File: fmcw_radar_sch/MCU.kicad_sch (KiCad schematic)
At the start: 0 parts

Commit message: minor changes
minorchanges
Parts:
- added U1: STM32F100CBTx, Package_QFP:LQFP-48_7x7mm_P0.5mm, symbol MCU_ST_STM32F1:STM32F100CBTx
- added U2: ADF4372BCCZ, CC-48-4_ADI, symbol Analog Devices:ADF4372BCCZ
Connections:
- new net: U1.23 (VSS), U1.35 (VSS), U1.47 (VSS)

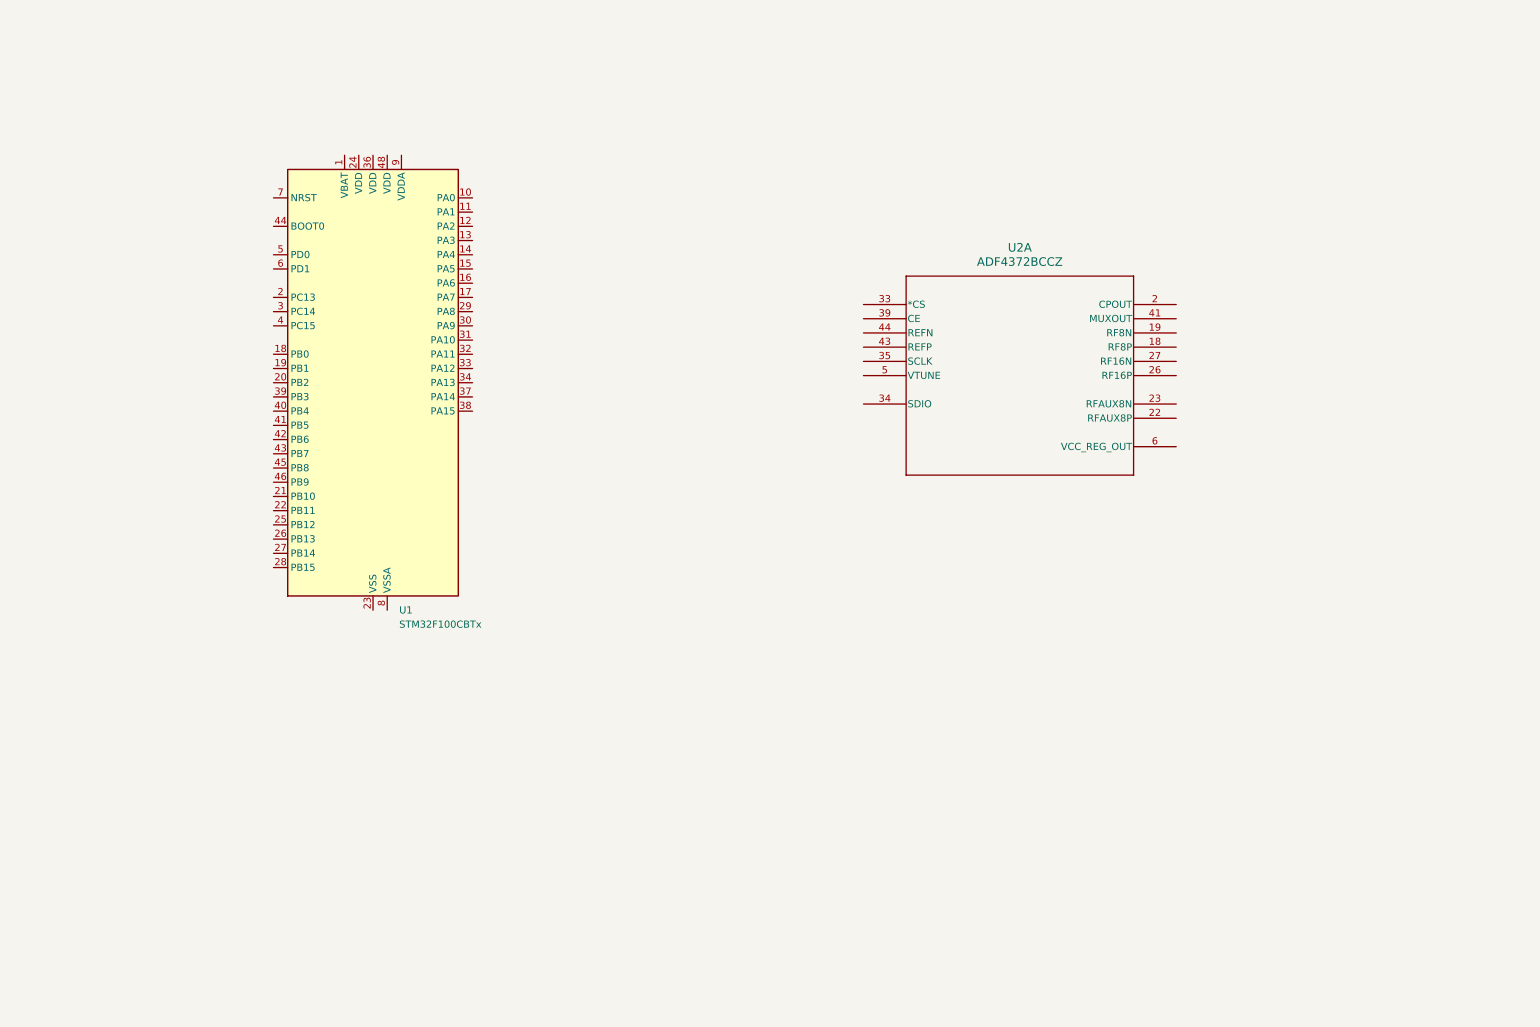
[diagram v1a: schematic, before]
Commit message: added MCU PSU VCO
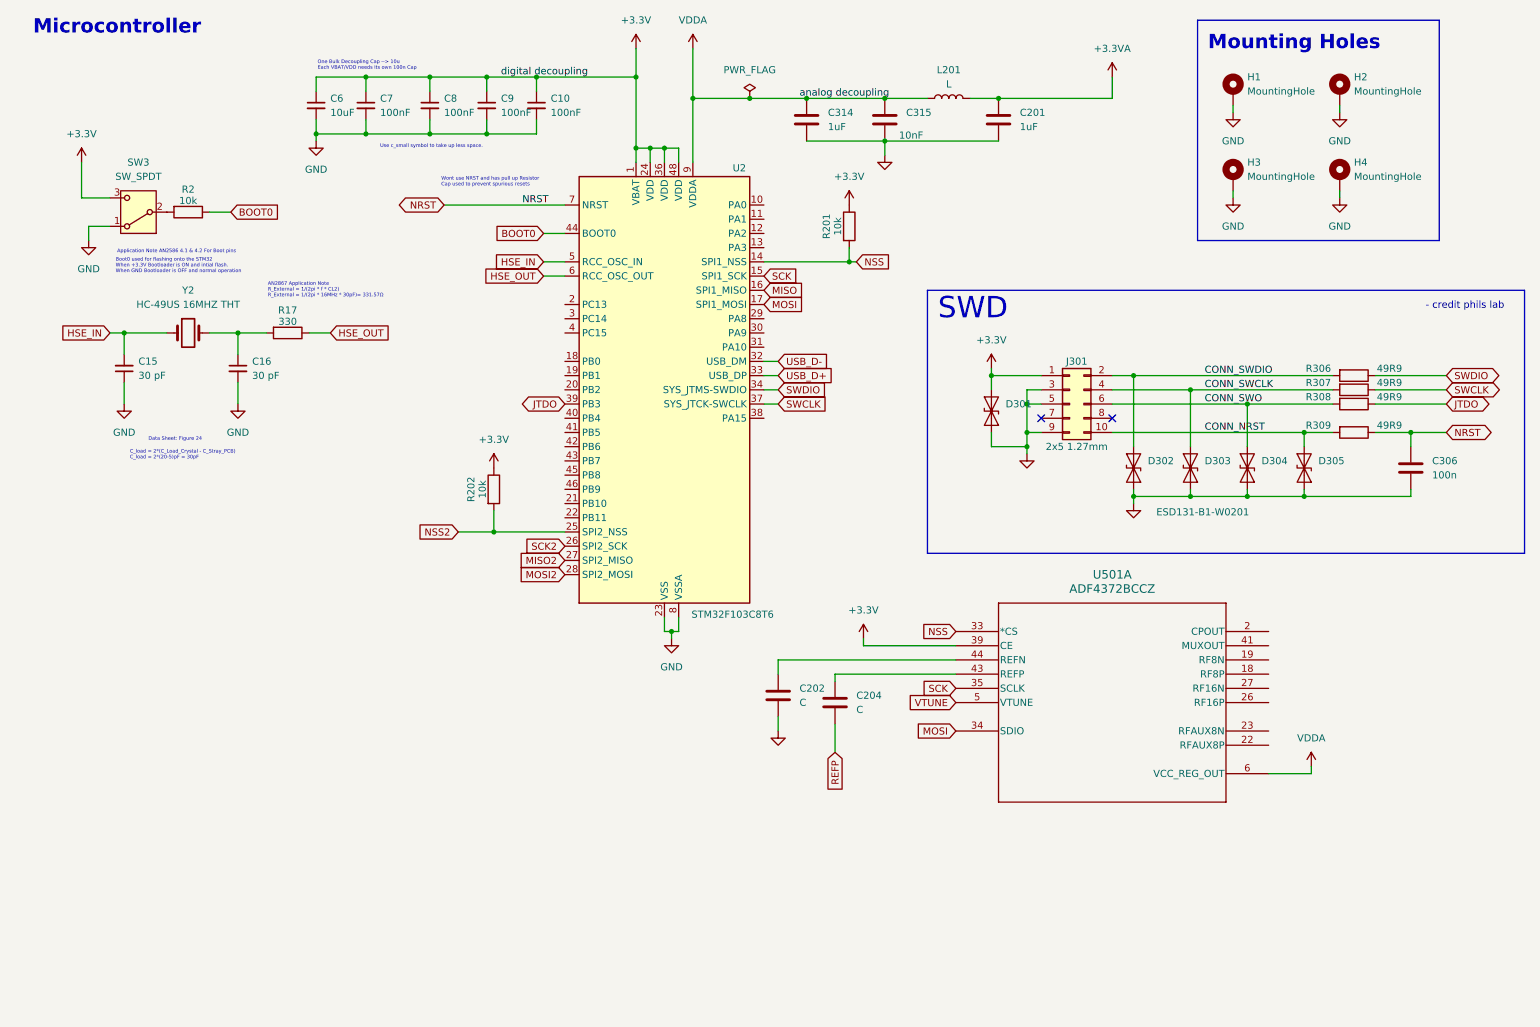
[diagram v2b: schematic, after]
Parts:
- removed U1: STM32F100CBTx, Package_QFP:LQFP-48_7x7mm_P0.5mm, symbol MCU_ST_STM32F1:STM32F100CBTx
- removed U2: ADF4372BCCZ, CC-48-4_ADI, symbol Analog Devices:ADF4372BCCZ
- added C10, C7, C8, C9: 100nF, Capacitor_SMD:C_1206_3216Metric_Pad1.33x1.80mm_HandSolder, symbol Device:C_Small
- added C15, C16: 30 pF, Capacitor_SMD:C_1206_3216Metric_Pad1.33x1.80mm_HandSolder, symbol Device:C_Small
- added C201, C314: 1uF, Capacitor_SMD:C_0603_1608Metric_Pad1.08x0.95mm_HandSolder, symbol Device:C
- added C202, C204: C, symbol Device:C
- added C306: 100n, Capacitor_SMD:C_0603_1608Metric_Pad1.08x0.95mm_HandSolder, symbol Device:C
- added C315: 10nF, Capacitor_SMD:C_0603_1608Metric_Pad1.08x0.95mm_HandSolder, symbol Device:C
- added C6: 10uF, Capacitor_SMD:C_1206_3216Metric_Pad1.33x1.80mm_HandSolder, symbol Device:C_Small
- added D301, D302, D303, D304, D305: ESD131-B1-W0201, Diode_SMD:Nexperia_DSN0603-2_0.6x0.3mm_P0.4mm, symbol Diode:ESD131-B1-W0201
- added H1, H2, H3, H4: MountingHole, MountingHole:MountingHole_3.2mm_M3_Pad, symbol Mechanical:MountingHole_Pad
- added J301: 2x5 1.27mm, Connector_PinHeader_2.54mm:PinHeader_2x05_P2.54mm_Vertical, symbol Connector_Generic:Conn_02x05_Odd_Even
- added L201: L, symbol Device:L
- added R17: 330, Resistor_SMD:R_1206_3216Metric_Pad1.30x1.75mm_HandSolder, symbol Device:R
- added R2, R201, R202: 10k, Resistor_SMD:R_1206_3216Metric_Pad1.30x1.75mm_HandSolder, symbol Device:R
- added R306, R307, R308, R309: 49R9, Resistor_SMD:R_0603_1608Metric_Pad0.98x0.95mm_HandSolder, symbol Device:R
- added SW3: SW_SPDT, Button_Switch_THT:SW_Slide_SPDT_Straight_CK_OS102011MS2Q, symbol Switch:SW_SPDT
- added U2: STM32F103C8T6, Package_QFP:LQFP-48_7x7mm_P0.5mm, symbol MCU_ST_STM32F1:STM32F103C8Tx
- added U501: ADF4372BCCZ, CC-48-4_ADI, symbol Analog Devices:ADF4372BCCZ
- added Y2: HC-49US 16MHZ THT, Crystal:Crystal_HC49-4H_Vertical, symbol Device:Crystal
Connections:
- new net: R2.2, SW3.2 (B)
- new net: C16.1, R17.2, Y2.2
- new net: C202.1, U501.44 (REFN)
- new net: C204.1, U501.43 (REFP)
- new net +3.3V: C10.1, C6.1, C7.1, C8.1, C9.1, D301.2 (A2), J301.1 (Pin_1), R201.1, R202.1, SW3.3 (C), U2.1 (VBAT), U2.24 (VDD), U2.36 (VDD), U2.48 (VDD), U501.39 (CE)
- new net +3.3VA: C201.1, L201.2
- new net BOOT0: R2.1, U2.44 (BOOT0)
- new net CONN_NRST: D305.2 (A2), J301.10 (Pin_10), R309.2
- new net CONN_SWCLK: D303.2 (A2), J301.4 (Pin_4), R307.2
- new net CONN_SWDIO: D302.2 (A2), J301.2 (Pin_2), R306.2
- new net CONN_SWO: D304.2 (A2), J301.6 (Pin_6), R308.2
- new net GND: C10.2, C15.1, C16.2, C201.2, C202.2, C306.2, C314.2, C315.2, C6.2, C7.2, C8.2, C9.2, D301.1 (A1), D302.1 (A1), D303.1 (A1), D304.1 (A1), D305.1 (A1), H1.1, H2.1, H3.1, H4.1, J301.3 (Pin_3), J301.5 (Pin_5), J301.9 (Pin_9), SW3.1 (A), U2.23 (VSS), U2.35 (VSS), U2.47 (VSS), U2.8 (VSSA)
- new net HSE_IN: C15.2, U2.5 (PD0), Y2.1
- new net HSE_OUT: R17.1, U2.6 (PD1)
- new net JTDO: R308.1, U2.39 (PB3)
- new net MISO: U2.16 (PA6)
- new net MISO2: U2.27 (PB14)
- new net MOSI: U2.17 (PA7), U501.34 (SDIO)
- new net MOSI2: U2.28 (PB15)
- new net NRST: C306.1, R309.1, U2.7 (NRST)
- new net NSS: R201.2, U2.14 (PA4), U501.33 (*CS)
- new net NSS2: R202.2, U2.25 (PB12)
- new net REFP: C204.2
- new net SCK: U2.15 (PA5), U501.35 (SCLK)
- new net SCK2: U2.26 (PB13)
- new net SWCLK: R307.1, U2.37 (PA14)
- new net SWDIO: R306.1, U2.34 (PA13)
- new net USB_D+: U2.33 (PA12)
- new net USB_D-: U2.32 (PA11)
- new net VDDA: C314.1, C315.1, L201.1, U2.9 (VDDA), U501.6 (VCC_REG_OUT)
- new net VTUNE: U501.5 (VTUNE)
- no-connect marks 0 -> 2
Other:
- note added: "- credit phils lab"
- note added: "AN2867 Application Note R_External = 1/(2pi * f * CL2) R_External = 1/(2pi * 16MHz * 30pF)= 331.57Ω"
- note added: "Application Note AN2586 4.1 & 4.2 For Boot pins"
- note added: "Boot0 used for flashing onto the STM32 When +3.3V Bootloader is ON and intial flash. When GND Bootloader is OFF and normal operation"
- note added: "C_load = 2*(C_Load_Crystal - C_Stray_PCB) C_load = 2*(20-5)pF = 30pF"
- note added: "Data Sheet: Figure 24"
- note added: "Microcontroller"
- note added: "Mounting Holes"
- note added: "One Bulk Decoupling Cap --> 10u Each VBAT/VDD needs its own 100n Cap"
- note added: "SWD"
- note added: "Use c_small symbol to take up less space."
- note added: "Wont use NRST and has pull up Resistor Cap used to prevent spurious resets"

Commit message: board changes
board changes
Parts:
- removed C202, C204: C, symbol Device:C
- removed U501: ADF4372BCCZ, CC-48-4_ADI, symbol Analog Devices:ADF4372BCCZ
- L201: value L -> 10n
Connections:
- net DAC_NCLR: now reaches U2.20 (PB2)
- net DAC_NLDAC: now reaches U2.21 (PB10)
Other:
- note removed: "- credit phils lab"
- moved on the sheet: R202

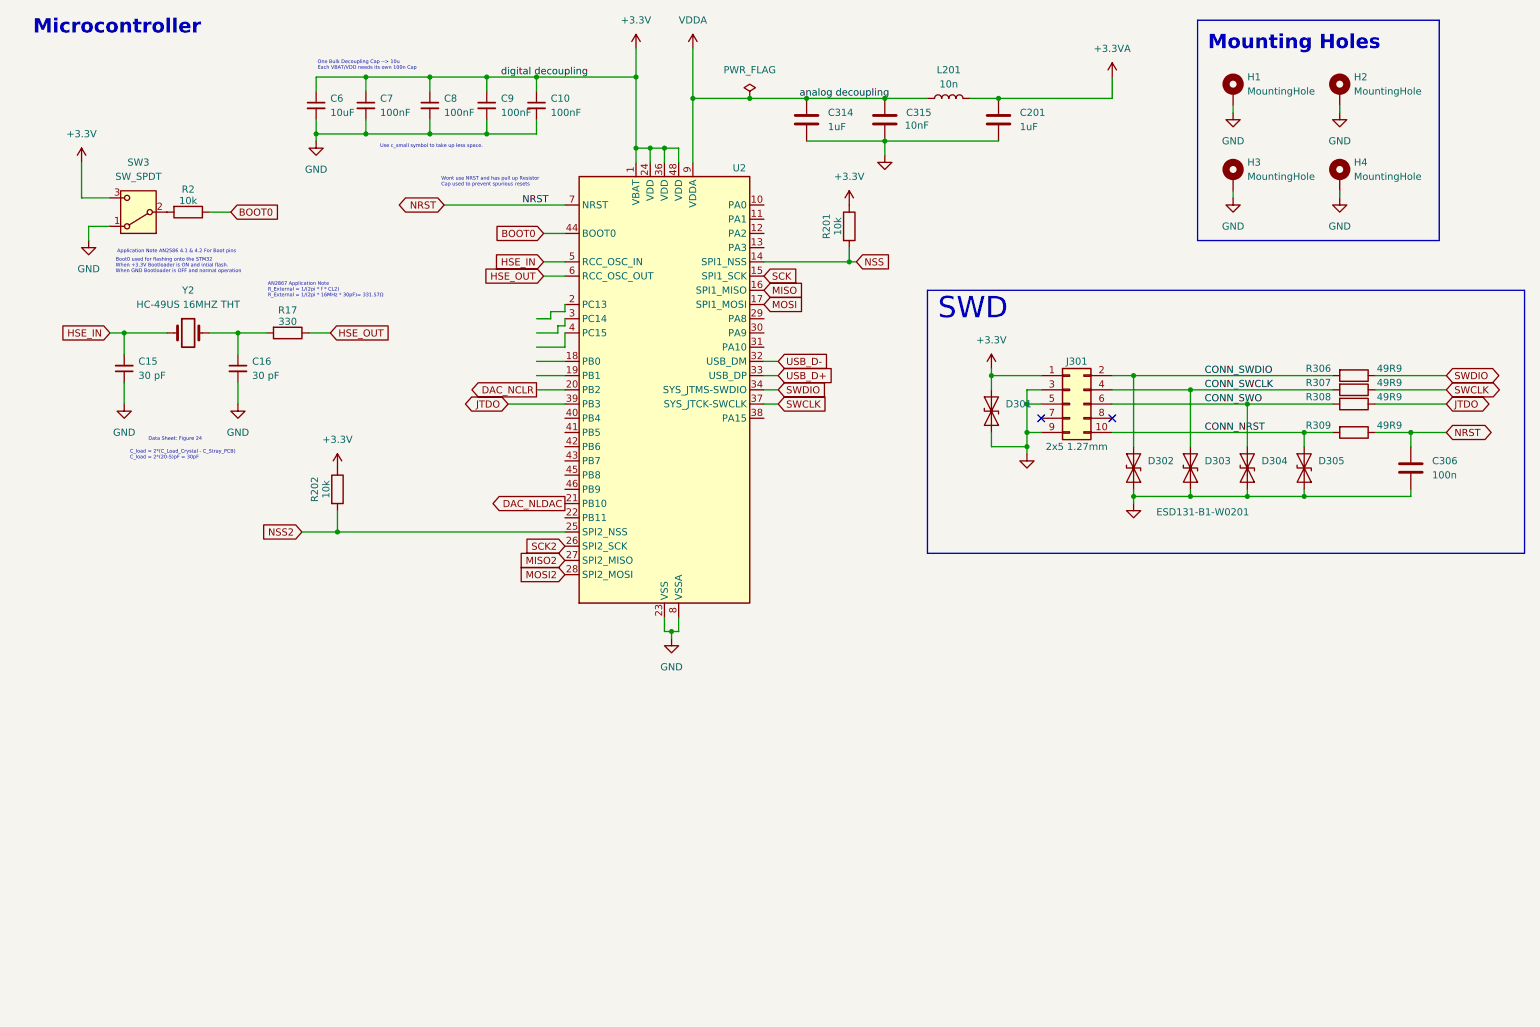
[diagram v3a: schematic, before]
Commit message: Layout of controller board
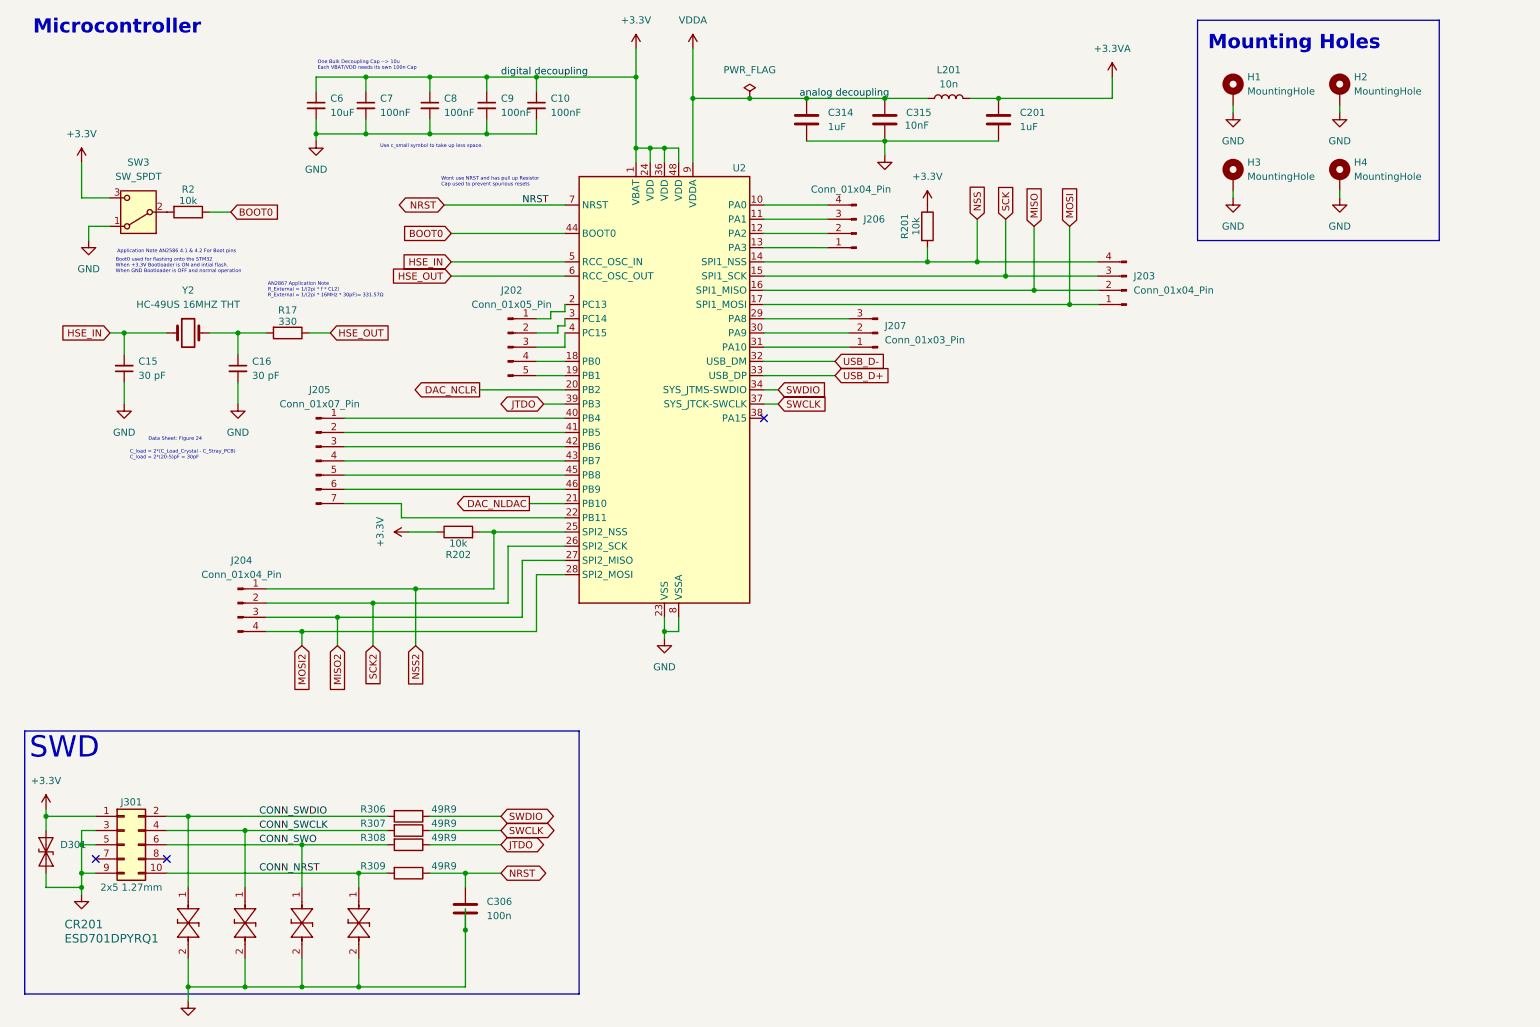
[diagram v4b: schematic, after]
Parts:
- removed D302, D303, D304, D305: ESD131-B1-W0201, Diode_SMD:Nexperia_DSN0603-2_0.6x0.3mm_P0.4mm, symbol Diode:ESD131-B1-W0201
- added CR201, CR202, CR203, CR204: ESD701DPYRQ1, nonkicad:X1SON2_DPY_TEX, symbol non_kicad:ESD701DPYRQ1
- added J202: Conn_01x05_Pin, Connector_PinHeader_2.54mm:PinHeader_1x05_P2.54mm_Vertical, symbol Connector:Conn_01x05_Pin
- added J203, J204, J206: Conn_01x04_Pin, Connector_PinHeader_2.54mm:PinHeader_1x04_P2.54mm_Vertical, symbol Connector:Conn_01x04_Pin
- added J205: Conn_01x07_Pin, Connector_PinHeader_2.54mm:PinHeader_1x07_P2.54mm_Vertical, symbol Connector:Conn_01x07_Pin
- added J207: Conn_01x03_Pin, Connector_PinHeader_2.54mm:PinHeader_1x03_P2.54mm_Vertical, symbol Connector:Conn_01x03_Pin
- L201: footprint (none) -> Inductor_SMD:L_1206_3216Metric
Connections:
- net CONN_NRST: now also CR204.1
- net CONN_SWCLK: now also CR202.1
- net CONN_SWDIO: now also CR201.1
- net CONN_SWO: now also CR203.1
- net GND: now also CR201.2, CR202.2, CR203.2, CR204.2
- net MISO: now also J203.2 (Pin_2)
- net MISO2: now also J204.3 (Pin_3)
- net MOSI: now also J203.1 (Pin_1)
- net MOSI2: now also J204.4 (Pin_4)
- net NSS: now also J203.4 (Pin_4)
- net NSS2: now also J204.1 (Pin_1)
- net SCK: now also J203.3 (Pin_3)
- net SCK2: now also J204.2 (Pin_2)
- net at U2.10 (PA0): now also J206.4 (Pin_4)
- net at U2.11 (PA1): now also J206.3 (Pin_3)
- net at U2.12 (PA2): now also J206.2 (Pin_2)
- net at U2.13 (PA3): now also J206.1 (Pin_1)
- net at U2.18 (PB0): now also J202.4 (Pin_4)
- net at U2.19 (PB1): now also J202.5 (Pin_5)
- net at U2.2 (PC13): now also J202.1 (Pin_1)
- net at U2.22 (PB11): now also J205.7 (Pin_7)
- net at U2.29 (PA8): now also J207.3 (Pin_3)
- net at U2.3 (PC14): now also J202.2 (Pin_2)
- net at U2.30 (PA9): now also J207.2 (Pin_2)
- net at U2.31 (PA10): now also J207.1 (Pin_1)
- net at U2.4 (PC15): now also J202.3 (Pin_3)
- net at U2.40 (PB4): now also J205.1 (Pin_1)
- net at U2.41 (PB5): now also J205.2 (Pin_2)
- net at U2.42 (PB6): now also J205.3 (Pin_3)
- net at U2.43 (PB7): now also J205.4 (Pin_4)
- net at U2.45 (PB8): now also J205.5 (Pin_5)
- net at U2.46 (PB9): now also J205.6 (Pin_6)
- no-connect marks 2 -> 3
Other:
- moved on the sheet: C306, D301, J301, R201, R202, R306, R307, R308, R309

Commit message: CHANGES
changes
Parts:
- renumbered C15 to C1, C315 to C10, C201 to C11, C16 to C2, C6 to C3, C7 to C4, C8 to C5, C306 to C6, C9 to C7, C10 to C8, C314 to C9, CR201 to CR1, CR202 to CR2, CR203 to CR3, CR204 to CR4, D301 to D1, H3 to H2, H2 to H3, J301 to J1, J204 to J2, J205 to J3, J202 to J4, J206 to J5, J207 to J6, J203 to J7, L201 to L1, R2 to R1, R17 to R2, R306 to R3, R307 to R4, R308 to R5, R309 to R6, R202 to R7, R201 to R8, SW3 to SW1, U2 to U1, Y2 to Y1

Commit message: changes
changes
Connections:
- net NRST: no longer C6.1, R6.1
- new net: C6.1, R6.1
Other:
- moved on the sheet: C6, CR1, D1, J1, R3, R4, R5, R6

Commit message: a lot of updates
usb power delivery + finishing touches
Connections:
- net NRST: now also C6.1, R6.1
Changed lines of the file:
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@@
+	)
+	(junction
+		(at 257.81 134.62)
+		(diameter 0)
+		(color 0 0 0 0)
 	)
 	(junction
@@
 		)
 		(stroke
+			(width 0)
+			(type default)
+		)
+	)
+	(wire
+		(pts
+			(xy 257.81 134.62) (xy 264.16 134.62)
+		)
+		(stroke
